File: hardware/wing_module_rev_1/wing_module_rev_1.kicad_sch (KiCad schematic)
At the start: 64 parts, among them J1 STRAIN, J2 TORSION, J3 Conn_01x03, J4 Conn_01x03, J5 Conn_01x04, J6 Conn_ST_STDC14, J7 Conn_01x04, J8 Conn_01x04, U1 ADS131M03IRUK, U2 STM32F103T8U6, U3 TCAN3403, U4 TPS563201, U5 TPS7A8101, U6 BL9161G-33

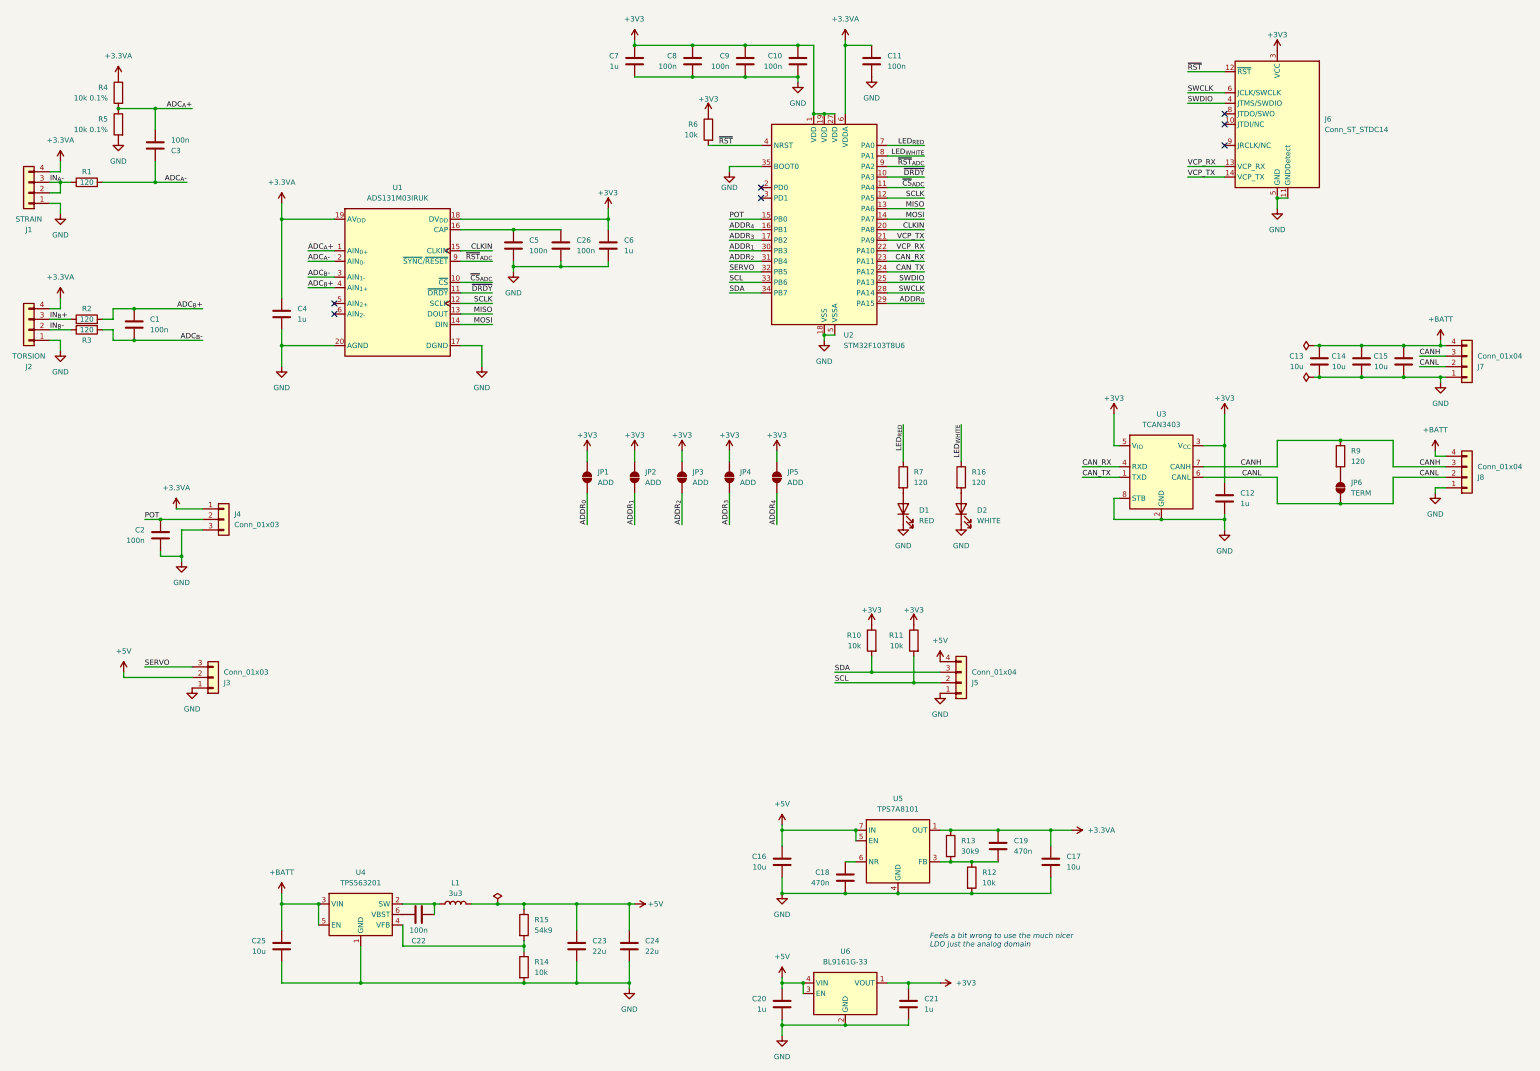
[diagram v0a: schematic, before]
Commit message: Split up schematic into multple pages, added CS pullup for ADC
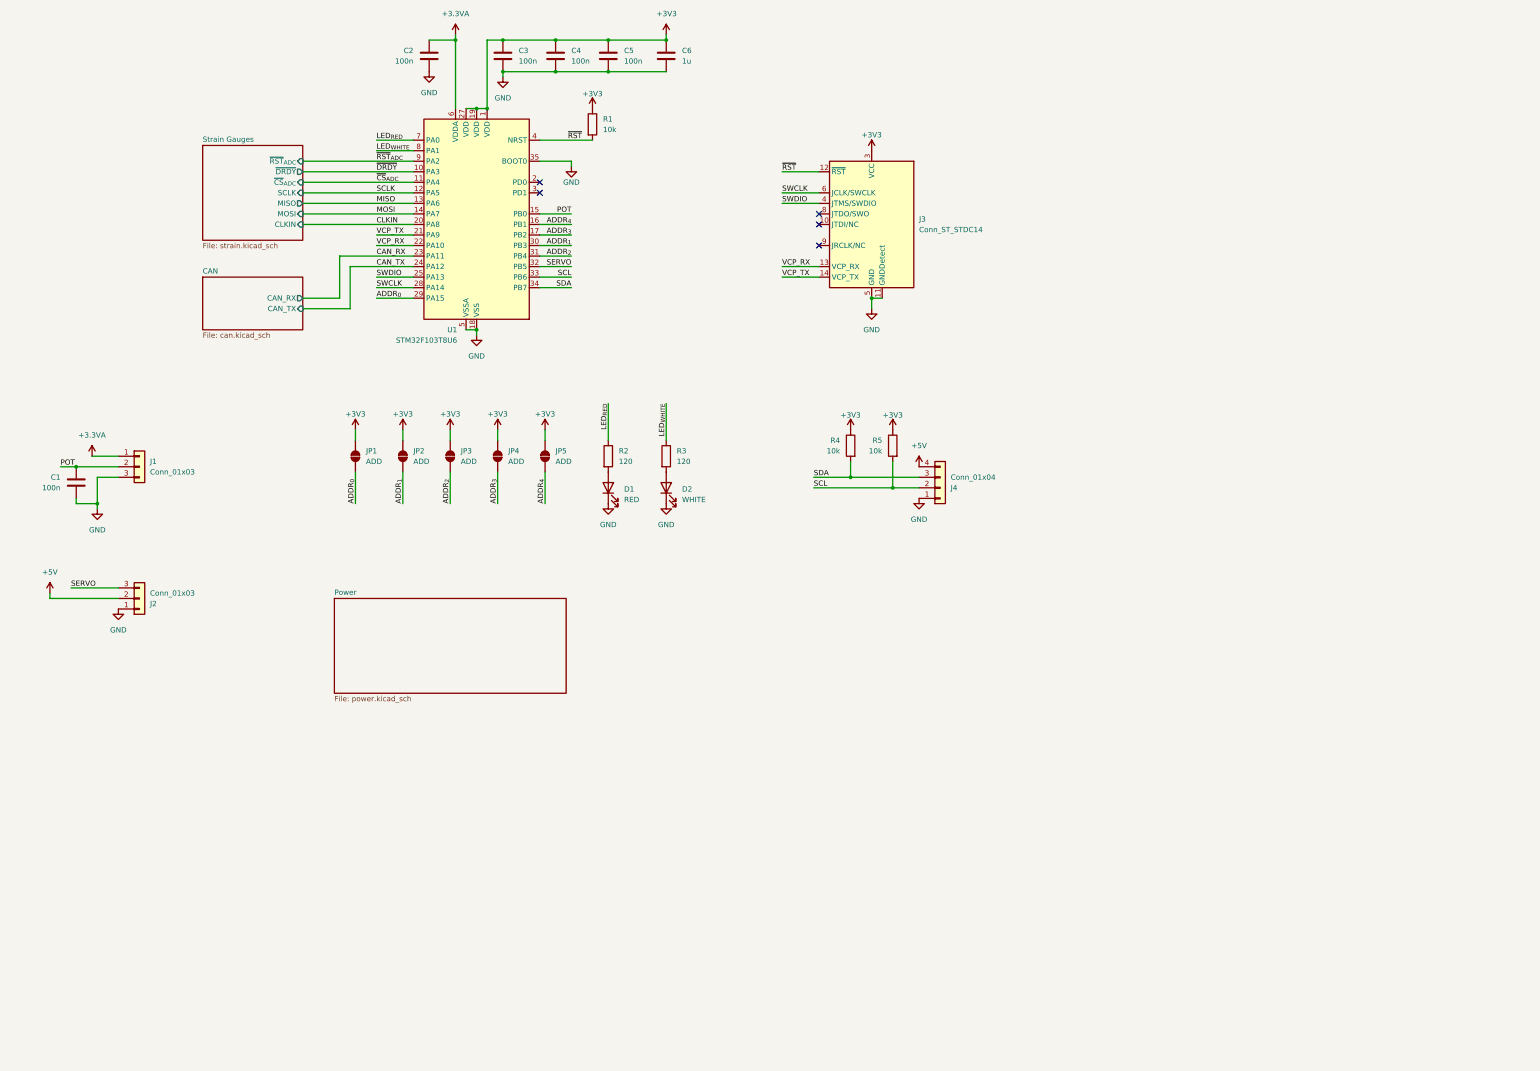
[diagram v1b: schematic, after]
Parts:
- removed C1, C22, C26, C3, C5: 100n, Capacitor_SMD:C_0402_1005Metric, symbol Device:C
- removed C12, C20, C21, C4, C6: 1u, Capacitor_SMD:C_0402_1005Metric, symbol Device:C
- removed C13, C14, C15, C16, C17, C25: 10u, Capacitor_SMD:C_0603_1608Metric, symbol Device:C
- removed C18, C19: 470n, Capacitor_SMD:C_0402_1005Metric, symbol Device:C
- removed C23, C24: 22u, Capacitor_SMD:C_0603_1608Metric, symbol Device:C
- removed J1: STRAIN, Connector_PinHeader_2.00mm:PinHeader_1x04_P2.00mm_Vertical, symbol Connector_Generic:Conn_01x04
- removed J2: TORSION, Connector_PinHeader_2.00mm:PinHeader_1x04_P2.00mm_Vertical, symbol Connector_Generic:Conn_01x04
- removed J7, J8: Conn_01x04, Connector_JST:JST_EH_B4B-EH-A_1x04_P2.50mm_Vertical, symbol Connector_Generic:Conn_01x04
- removed JP6: TERM, Jumper:SolderJumper-2_P1.3mm_Open_TrianglePad1.0x1.5mm, symbol Jumper:SolderJumper_2_Open
- removed L1: 3u3, Inductor_SMD:L_Changjiang_FNR6045S, symbol Device:L
- removed R1, R2, R3, R9: 120, Resistor_SMD:R_0402_1005Metric, symbol Device:R
- removed R12, R14: 10k, Resistor_SMD:R_0402_1005Metric, symbol Device:R
- removed R13: 30k9, Resistor_SMD:R_0402_1005Metric, symbol Device:R
- removed R15: 54k9, Resistor_SMD:R_0402_1005Metric, symbol Device:R
- removed R4, R5: 10k 0.1%, Resistor_SMD:R_0402_1005Metric, symbol Device:R
- removed U1: ADS131M03IRUK, Package_DFN_QFN:WQFN-20-1EP_3x3mm_P0.4mm_EP1.7x1.7mm, symbol wing_module:ADS131M03IRUK
- removed U3: TCAN3403, Package_TO_SOT_SMD:TSOT-23-8, symbol wing_module:TCAN3403
- removed U4: TPS563201, Package_TO_SOT_SMD:SOT-23-6, symbol wing_module:TPS563201
- removed U5: TPS7A8101, Package_SON:VSON-8-1EP_3x3mm_P0.65mm_EP1.65x2.4mm, symbol wing_module:TPS7A8101
- removed U6: BL9161G-33, Package_DFN_QFN:UDFN-4-1EP_1x1mm_P0.65mm_EP0.48x0.48mm, symbol wing_module:BL9161G
- renumbered C2 to C1, C11 to C2, C10 to C3, C9 to C4, C8 to C5, C7 to C6, J4 to J1, J3 to J2, J6 to J3, J5 to J4, R6 to R1, R7 to R2, R16 to R3, R10 to R4, R11 to R5, U2 to U1
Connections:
- net AGND renamed GND
- no-connect marks 7 -> 5
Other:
- added sheet CAN (can.kicad_sch)
- added sheet Power (power.kicad_sch)
- added sheet Strain Gauges (strain.kicad_sch)
- note removed: "Feels a bit wrong to use the much nicer LDO just the analog domain"
- company: (none) -> Savo Bajic
- title: (none) -> Wing Module
- moved on the sheet: C1, C2, C3, C4, C5, C6, D1, D2, J1, J2, J3, J4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

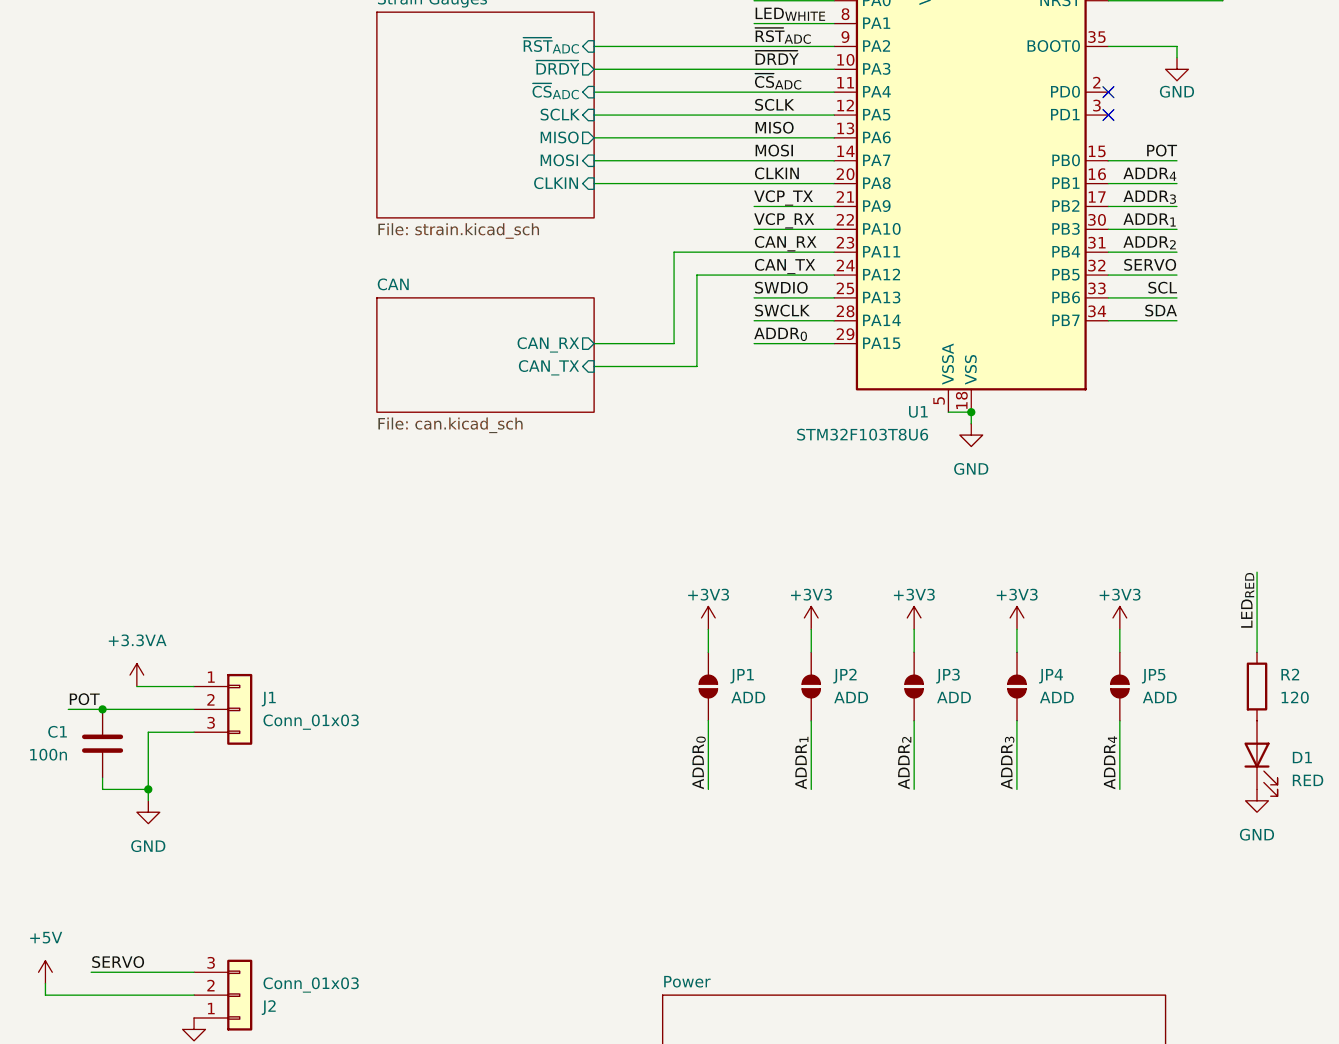
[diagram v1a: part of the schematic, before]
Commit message: Finished rev 1.0 layout of CAN
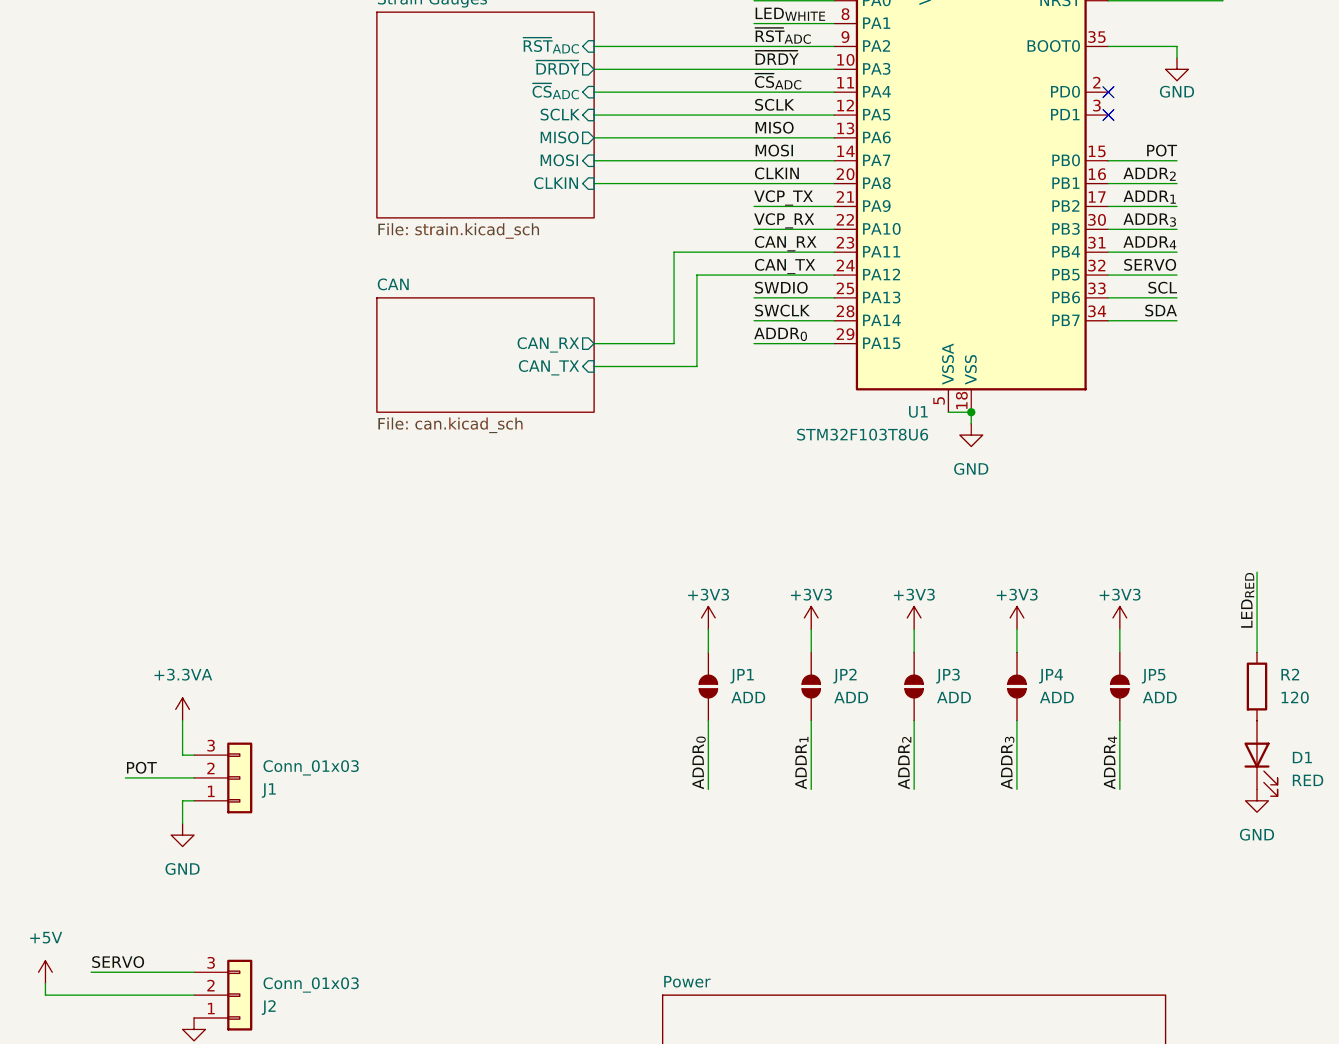
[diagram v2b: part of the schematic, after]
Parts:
- removed C1: 100n, Capacitor_SMD:C_0402_1005Metric, symbol Device:C
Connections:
- net +3.3VA: now also J1.3 (Pin_3); no longer J1.1 (Pin_1)
- net ADDR_{1}: now also U1.17 (PB2); no longer U1.30 (PB3)
- net ADDR_{2}: now also U1.16 (PB1); no longer U1.31 (PB4)
- net ADDR_{3}: now also U1.30 (PB3); no longer U1.17 (PB2)
- net ADDR_{4}: now also U1.31 (PB4); no longer U1.16 (PB1)
- net GND: now also J1.1 (Pin_1); no longer J1.3 (Pin_3)
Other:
- moved on the sheet: J1
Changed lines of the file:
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@@
 	)
 	(junction
-		(at 54.61 142.24)
-		(diameter 0)
-		(color 0 0 0 0)
-	)
-	(junction
 		(at 191.77 30.48)
 		(diameter 0)
@@
 		(color 0 0 0 0)
 	)
-	(junction
-		(at 49.53 133.35)
-		(diameter 0)
-		(color 0 0 0 0)
-	)
 	(no_connect
 		(at 161.29 67.31)
@@
 	(wire
 		(pts
-			(xy 45.72 133.35) (xy 49.53 133.35)
-		)
-		(stroke
-			(width 0)
-			(type default)
-		)
-	)
-	(wire
-		(pts
 			(xy 104.14 92.71) (xy 113.03 92.71)
 		)
@@
 	(wire
 		(pts
-			(xy 54.61 143.51) (xy 54.61 142.24)
-		)
-		(stroke
-			(width 0)
-			(type default)
-		)
-	)
-	(wire
-		(pts
 			(xy 241.3 95.25) (xy 241.3 92.71)
 		)
@@
 	(wire
 		(pts
-			(xy 49.53 140.97) (xy 49.53 142.24)
+			(xy 58.42 138.43) (xy 59.69 138.43)
 		)
 		(stroke
@@
 	(wire
 		(pts
-			(xy 53.34 130.81) (xy 59.69 130.81)
-		)
-		(stroke
-			(width 0)
-			(type default)
-		)
-	)
-	(wire
-		(pts
 			(xy 219.71 62.23) (xy 228.6 62.23)
 		)
@@
 	(wire
 		(pts
-			(xy 54.61 142.24) (xy 54.61 135.89)
+			(xy 58.42 143.51) (xy 58.42 146.05)
 		)
 		(stroke
@@
 	(wire
 		(pts
-			(xy 54.61 135.89) (xy 59.69 135.89)
+			(xy 58.42 143.51) (xy 59.69 143.51)
 		)
 		(stroke
@@
 	(wire
 		(pts
+			(xy 58.42 134.62) (xy 58.42 138.43)
+		)
+		(stroke
+			(width 0)
+			(type default)
+		)
+	)
+	(wire
+		(pts
 			(xy 165.1 38.1) (xy 152.4 38.1)
 		)
@@
 	(wire
 		(pts
-			(xy 49.53 133.35) (xy 59.69 133.35)
+			(xy 52.07 140.97) (xy 59.69 140.97)
 		)
 		(stroke
@@
 		)
 	)
-	(wire
-		(pts
-			(xy 49.53 142.24) (xy 54.61 142.24)
-		)
-		(stroke
-			(width 0)
-			(type default)
-		)
-	)
 	(label "~{CS}_{ADC}"
 		(at 121.92 64.77 0)
@@
 		)
 	)
+	(label "ADDR_{3}"
+		(at 168.91 80.01 180)
+		(effects
+			(font
+				(size 1.27 1.27)
+			)
+			(justify right bottom)
+		)
+	)
 	(label "~{RST}"
 		(at 219.71 62.23 0)
@@
 		)
 	)
+	(label "ADDR_{4}"
+		(at 168.91 82.55 180)
+		(effects
+			(font
+				(size 1.27 1.27)
+			)
+			(justify right bottom)
+		)
+	)
 	(label "SERVO"
 		(at 168.91 85.09 180)
@@
 		)
 	)
-	(label "ADDR_{3}"
-		(at 168.91 77.47 180)
-		(effects
-			(font
-				(size 1.27 1.27)
-			)
-			(justify right bottom)
-		)
-	)
-	(label "ADDR_{2}"
-		(at 168.91 82.55 180)
-		(effects
-			(font
-				(size 1.27 1.27)
-			)
-			(justify right bottom)
-		)
-	)
-	(label "ADDR_{1}"
-		(at 168.91 80.01 180)
-		(effects
-			(font
-				(size 1.27 1.27)
-			)
-			(justify right bottom)
-		)
-	)
 	(label "POT"
 		(at 168.91 72.39 180)
@@
 		)
 	)
-	(label "ADDR_{1}"
-		(at 128.27 142.24 90)
+	(label "ADDR_{2}"
+		(at 168.91 74.93 180)
 		(effects
 			(font
 				(size 1.27 1.27)
 			)
-			(justify left bottom)
+			(justify right bottom)
 		)
 	)
-	(label "ADDR_{4}"
-		(at 168.91 74.93 180)
+	(label "ADDR_{1}"
+		(at 128.27 142.24 90)
 		(effects
 			(font
 				(size 1.27 1.27)
 			)
-			(justify right bottom)
+			(justify left bottom)
 		)
 	)
@@
 		)
 	)
+	(label "ADDR_{1}"
+		(at 168.91 77.47 180)
+		(effects
+			(font
+				(size 1.27 1.27)
+			)
+			(justify right bottom)
+		)
+	)
 	(label "ADDR_{4}"
 		(at 162.56 142.24 90)
@@
 	)
 	(label "POT"
-		(at 45.72 133.35 0)
+		(at 52.07 140.97 0)
 		(effects
 			(font
@@
 	)
 	(symbol
-		(lib_id "Device:C")
-		(at 49.53 137.16 0)
-		(mirror y)
-		(unit 1)
-		(exclude_from_sim no)
-		(in_bom yes)
-		(on_board yes)
-		(dnp no)
-		(property "Reference" "C1"
-			(at 45.72 135.8899 0)
-			(effects
-				(font
-					(size 1.27 1.27)
-				)
-				(justify left)
-			)
-		)
-		(property "Value" "100n"
-			(at 45.72 138.4299 0)
-			(effects
-				(font
-					(size 1.27 1.27)
-				)
-				(justify left)
-			)
-		)
-		(property "Footprint" "Capacitor_SMD:C_0402_1005Metric"
-			(at 48.5648 140.97 0)
-			(effects
-				(font
-					(size 1.27 1.27)
-				)
-				(hide yes)
-			)
-		)
-		(property "Datasheet" "~"
-			(at 49.53 137.16 0)
-			(effects
-				(font
-					(size 1.27 1.27)
-				)
-				(hide yes)
-			)
-		)
-		(property "Description" "Unpolarized capacitor"
-			(at 49.53 137.16 0)
-			(effects
-				(font
-					(size 1.27 1.27)
-				)
-				(hide yes)
-			)
-		)
-		(property "LCSC" "C5448875"
-			(at 49.53 137.16 0)
-			(effects
-				(font
-					(size 1.27 1.27)
-				)
-				(hide yes)
-			)
-		)
-		(pin "1"
-		)
-		(pin "2"
-		)
-		(instances
-			(project "wing_module_rev_1"
-				(path "/7b7fffa9-e888-4279-94bf-385d74cf78f9"
-					(reference "C1")
-					(unit 1)
-				)
-			)
-		)
-	)
-	(symbol
 		(lib_id "power:+5V")
 		(at 43.18 163.83 0)
@@
 	(symbol
 		(lib_id "Connector_Generic:Conn_01x03")
-		(at 64.77 133.35 0)
+		(at 64.77 140.97 0)
+		(mirror x)
 		(unit 1)
 		(exclude_from_sim no)
@@
 		(on_board yes)
 		(dnp no)
-		(fields_autoplaced yes)
 		(property "Reference" "J1"
-			(at 67.31 132.0799 0)
+			(at 67.31 142.2401 0)
 			(effects
 				(font
@@
 		)
 		(property "Value" "Conn_01x03"
-			(at 67.31 134.6199 0)
+			(at 67.31 139.7001 0)
 			(effects
 				(font
@@
 		)
 		(property "Footprint" "Connector_JST:JST_EH_B3B-EH-A_1x03_P2.50mm_Vertical"
-			(at 64.77 133.35 0)
+			(at 64.77 140.97 0)
 			(effects
 				(font
@@
 		)
 		(property "Datasheet" "~"
-			(at 64.77 133.35 0)
+			(at 64.77 140.97 0)
 			(effects
 				(font
@@
 		)
 		(property "Description" "Generic connector, single row, 01x03, script generated (kicad-library-utils/schlib/autogen/connector/)"
-			(at 64.77 133.35 0)
+			(at 64.77 140.97 0)
 			(effects
 				(font
@@
 		)
 		(property "LCSC" "C398546"
-			(at 64.77 133.35 0)
+			(at 64.77 140.97 0)
 			(effects
 				(font
@@
 	(symbol
 		(lib_id "power:+3.3VA")
-		(at 53.34 130.81 0)
+		(at 58.42 134.62 0)
 		(unit 1)
 		(exclude_from_sim no)
@@
 		(fields_autoplaced yes)
 		(property "Reference" "#PWR02"
-			(at 53.34 134.62 0)
+			(at 58.42 138.43 0)
 			(effects
 				(font
@@
 		)
 		(property "Value" "+3.3VA"
-			(at 53.34 125.73 0)
+			(at 58.42 129.54 0)
 			(effects
 				(font
@@
 		)
 		(property "Footprint" ""
-			(at 53.34 130.81 0)
+			(at 58.42 134.62 0)
 			(effects
 				(font
@@
 		)
 		(property "Datasheet" ""
-			(at 53.34 130.81 0)
+			(at 58.42 134.62 0)
 			(effects
 				(font
@@
 		)
 		(property "Description" "Power symbol creates a global label with name \"+3.3VA\""
-			(at 53.34 130.81 0)
+			(at 58.42 134.62 0)
 			(effects
 				(font
@@
 	(symbol
 		(lib_id "power:GND")
-		(at 54.61 143.51 0)
+		(at 58.42 146.05 0)
 		(unit 1)
 		(exclude_from_sim no)
@@
 		(fields_autoplaced yes)
 		(property "Reference" "#PWR03"
-			(at 54.61 149.86 0)
+			(at 58.42 152.4 0)
 			(effects
 				(font
@@
 		)
 		(property "Value" "GND"
-			(at 54.61 148.59 0)
+			(at 58.42 151.13 0)
 			(effects
 				(font
@@
 		)
 		(property "Footprint" ""
-			(at 54.61 143.51 0)
+			(at 58.42 146.05 0)
 			(effects
 				(font
@@
 		)
 		(property "Datasheet" ""
-			(at 54.61 143.51 0)
+			(at 58.42 146.05 0)
 			(effects
 				(font
@@
 		)
 		(property "Description" "Power symbol creates a global label with name \"GND\" , ground"
-			(at 54.61 143.51 0)
+			(at 58.42 146.05 0)
 			(effects
 				(font
